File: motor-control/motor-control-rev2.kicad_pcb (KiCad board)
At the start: 2 copper layers, 122.3 x 65.9 mm, 80 parts, among them P1 CONN_02X12, P2 to_motor_phase_1, P3 to_motor_phase_2, P4 to_motor_phase_3, P5 CONN_01X01, P6 CONN_01X01, P7 CONN_01X04, Q1 csd19505kcs, Q10 csd19505kcs, Q11 csd19505kcs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

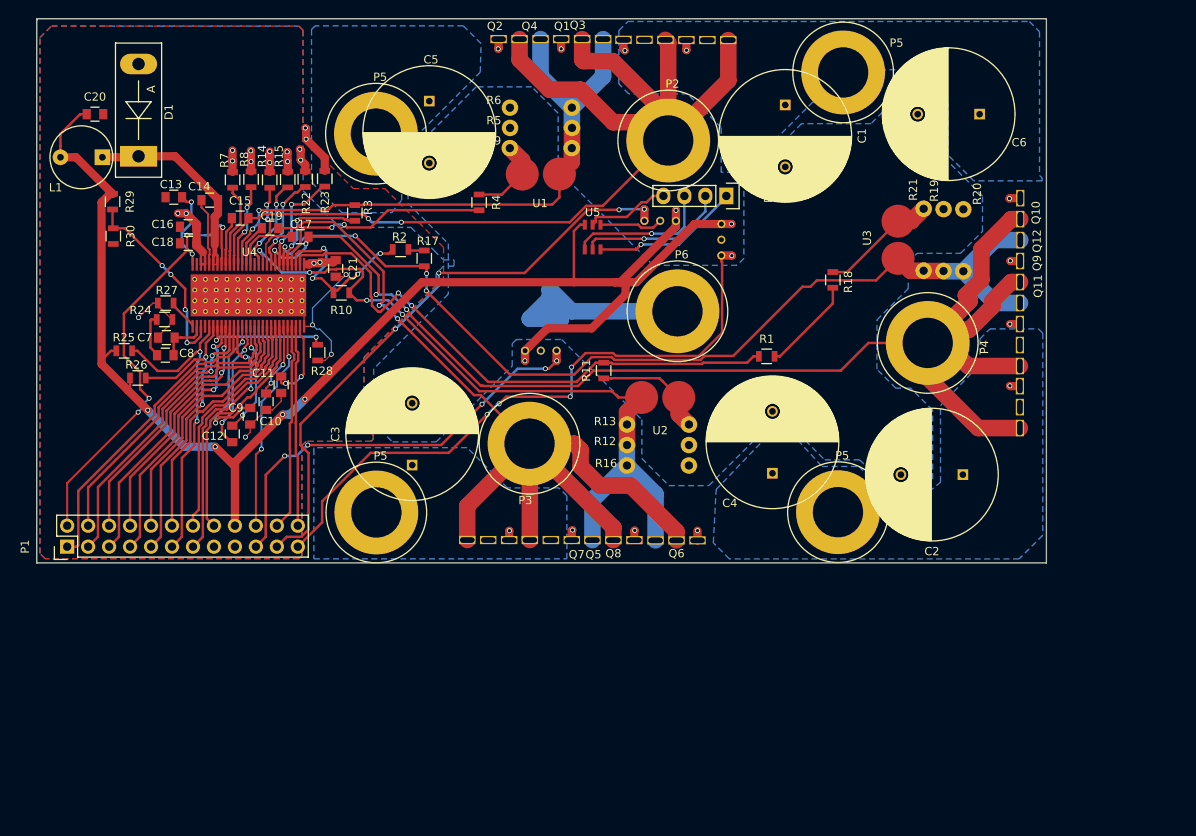
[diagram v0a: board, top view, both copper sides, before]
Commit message: Added dimensions & wire jumper #s
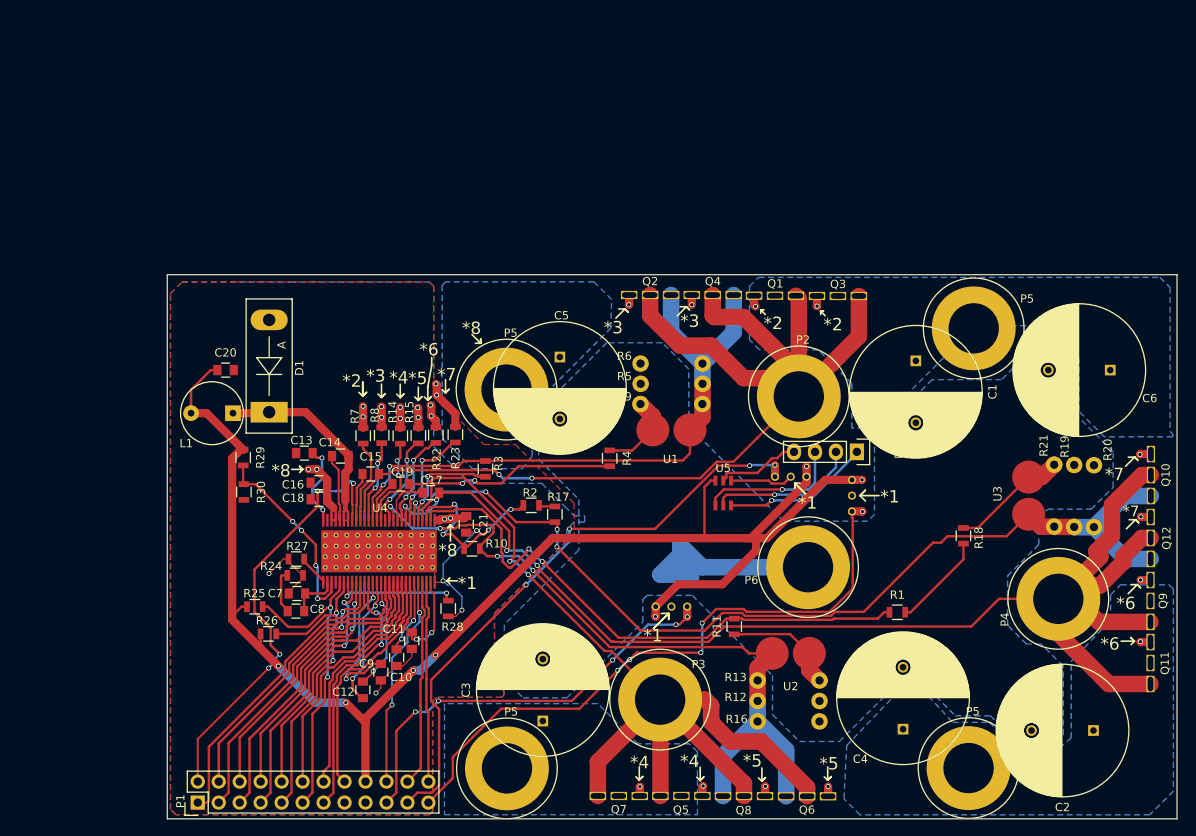
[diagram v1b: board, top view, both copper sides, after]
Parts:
- moved R20 34.8 mm to (202.6, 81.3)
- moved C17 34.8 mm to (122.3, 80.9)
- moved C4 34.8 mm to (179.5, 109.5)
- moved C7 34.8 mm to (106.1, 93.1)
- moved P5 34.8 mm to (187.4, 114.3)
- moved Q7 34.8 mm to (145.1, 117.6)
- moved R1 34.8 mm to (178.8, 95.4)
- moved R10 34.8 mm to (127.3, 87.7)
- moved R11 34.8 mm to (159.0, 97.1)
- moved R12 34.8 mm to (165.6, 106.1)
- moved R13 34.8 mm to (165.6, 103.6)
- moved R16 34.8 mm to (165.6, 108.6)
- moved R21 34.8 mm to (197.8, 81.3)
- moved R25 34.8 mm to (101.0, 94.7)
- moved R30 34.8 mm to (99.6, 80.8)
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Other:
- board text added: "*1"
- board text added: "*2"
- board text added: "*3"
- board text added: "*4"
- board text added: "*5"
- board text added: "*6"
- board text added: "*7"
- board text added: "*8"
- board text added: "12.28 cm"
- board text added: "6.61 cm"

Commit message: Modified Schematic Comp resist/cap vals, added bom
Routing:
- net (no net): track 0.00 -> 0.04 mm, vias 0 -> 1
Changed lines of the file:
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@@
     (thickness 1.6)
     (drawings 147)
-    (tracks 1263)
+    (tracks 1265)
     (zones 0)
     (modules 80)
@@
   (layers
     (0 F.Cu signal)
-    (31 B.Cu signal hide)
+    (31 B.Cu signal)
     (32 B.Adhes user)
     (33 F.Adhes user)
-    (34 B.Paste user hide)
+    (34 B.Paste user)
     (35 F.Paste user)
     (36 B.SilkS user)
     (37 F.SilkS user)
-    (38 B.Mask user hide)
+    (38 B.Mask user)
     (39 F.Mask user)
     (40 Dwgs.User user)
@@
   (gr_line (start 90.369 120.408) (end 90.369 54.749) (layer Edge.Cuts) (width 0.15))
   (gr_line (start 90.369 54.749) (end 90.369 54.622) (layer Edge.Cuts) (width 0.15))
+  (segment (start 106.62 87.18) (end 106.62 87.22) (width 0.1524) (layer F.Cu) (net 0))
+  (via (at 106.62 87.22) (size 0.6) (drill 0.4) (layers F.Cu B.Cu) (net 0))
   (segment (start 109.7172 79.32462) (end 108.771479 78.378899) (width 1) (layer F.Cu) (net 1))
   (segment (start 108.771479 78.378899) (end 108.47148 78.0789) (width 1) (layer F.Cu) (net 1))

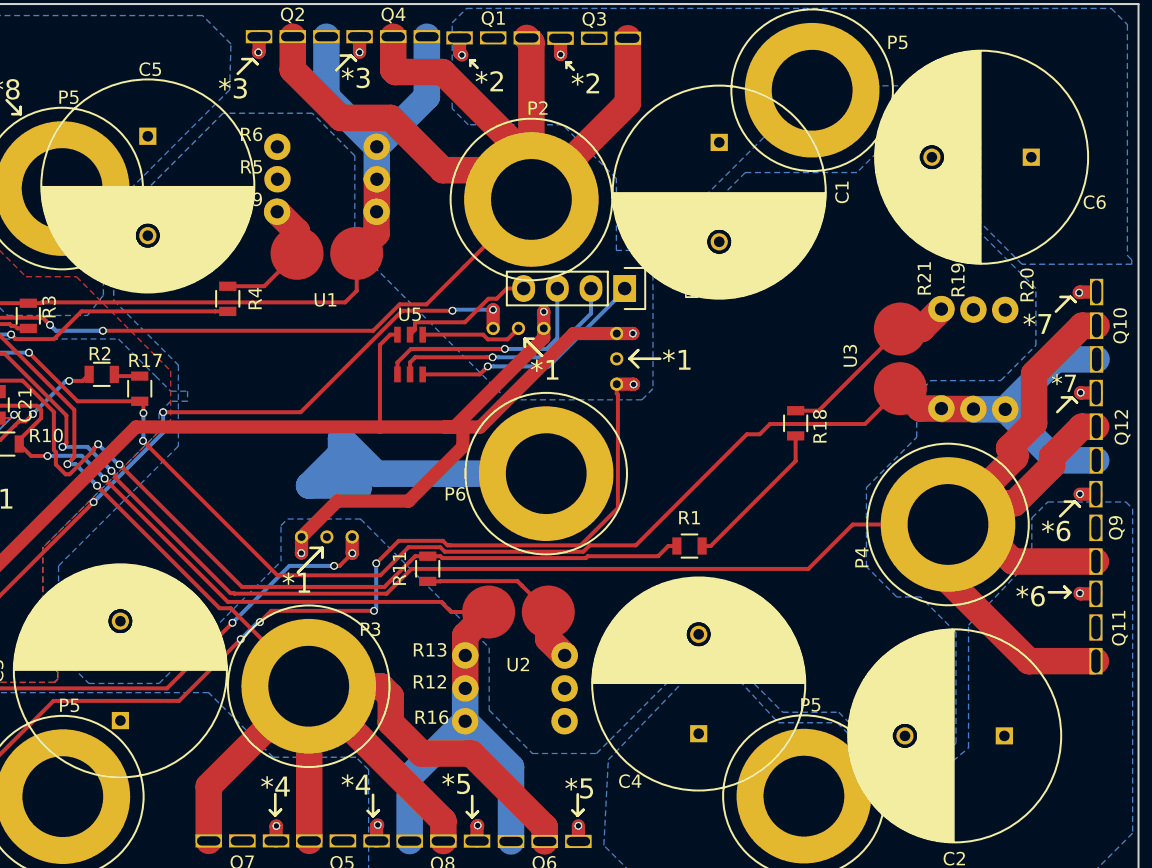
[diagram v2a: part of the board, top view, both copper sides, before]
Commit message: Modified hall footprint, began replacement in pcb
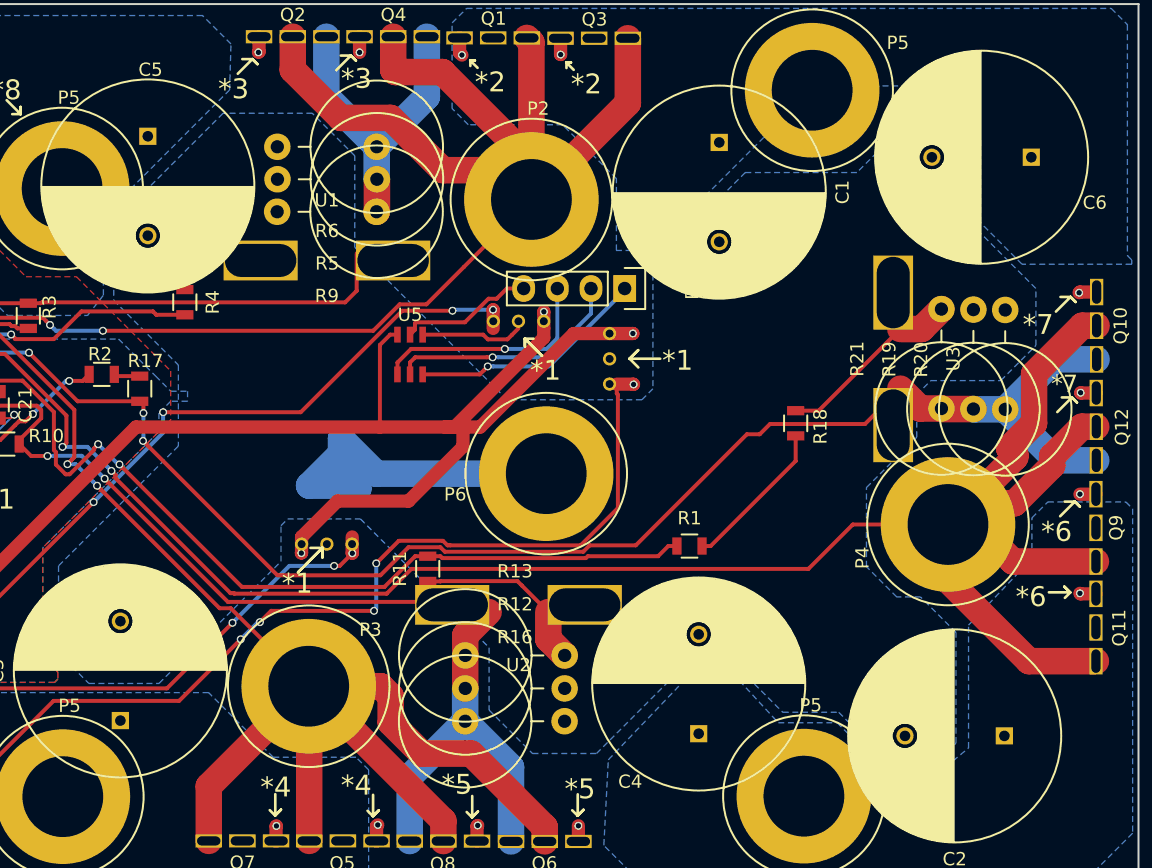
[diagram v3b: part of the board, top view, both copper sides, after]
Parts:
- C1, C2, C3, C4, C5, C6: value CP1 -> 470uF
- C21: value C_Small -> 4.7uF
- C7: value C_Small -> 2700 pF
- C8: value C_Small -> 6.8 pF
- R12, R13, R16, R19, R20, R21, R5, R6, R9: value R -> .33R; footprint p16261:Resistor_Vertical_RM7.5mm-edited -> Resistors_ThroughHole:Resistor_Vertical_RM7.5mm
- R24: value R -> 76.8k
- R28: value DNP -> 0R
- moved R4 3.25 mm to (140.7, 77.0)
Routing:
- net GND: track 107.1 -> 97.1 mm
- net /Gate-Driver/SL_A: track 75.7 -> 71.9 mm
- net /Gate-Driver/SP1: track 27.6 -> 24.5 mm
